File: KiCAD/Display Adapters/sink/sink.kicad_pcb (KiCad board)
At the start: 4 copper layers, 36.4 x 30.5 mm, 7 parts, among them J1 XT30PW_2_2_-M.G.B, J2 G46M2013201AWEU, J3 20455-040E-76

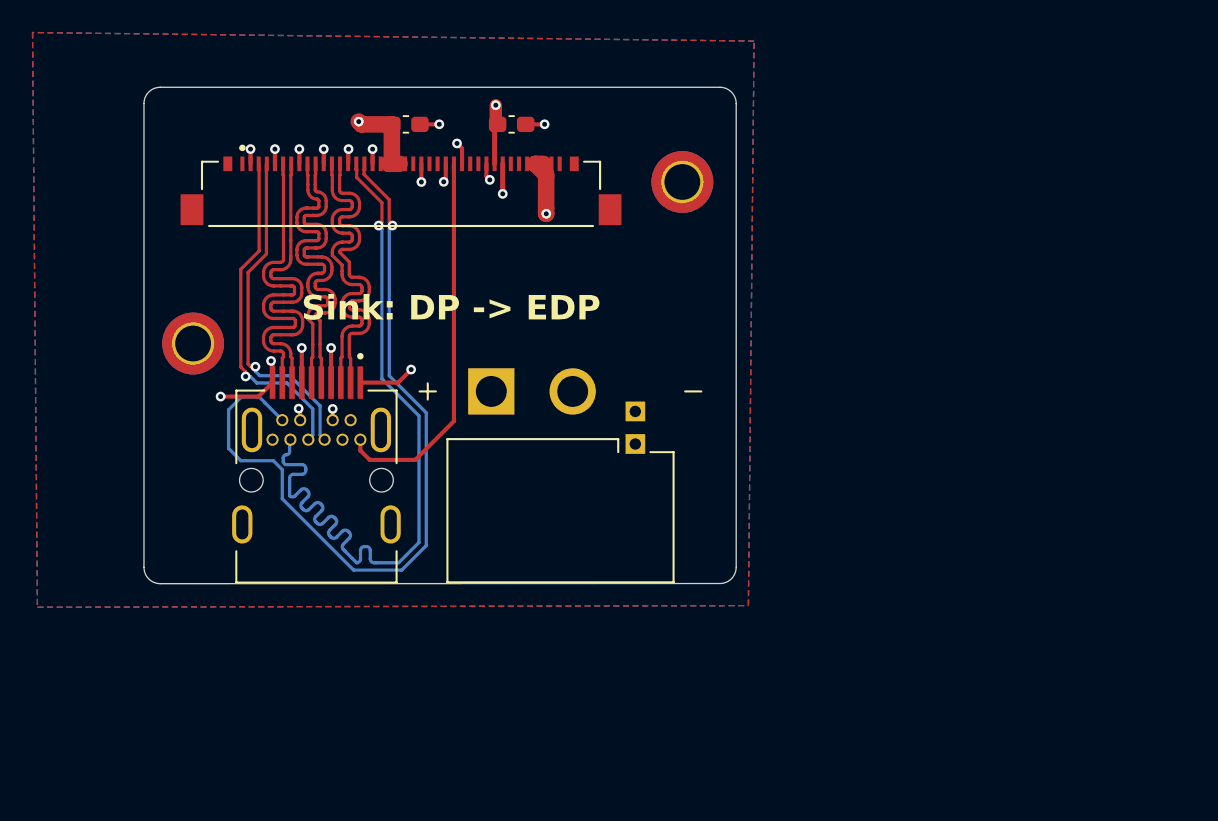
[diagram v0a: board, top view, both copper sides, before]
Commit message: use full sized dp instead
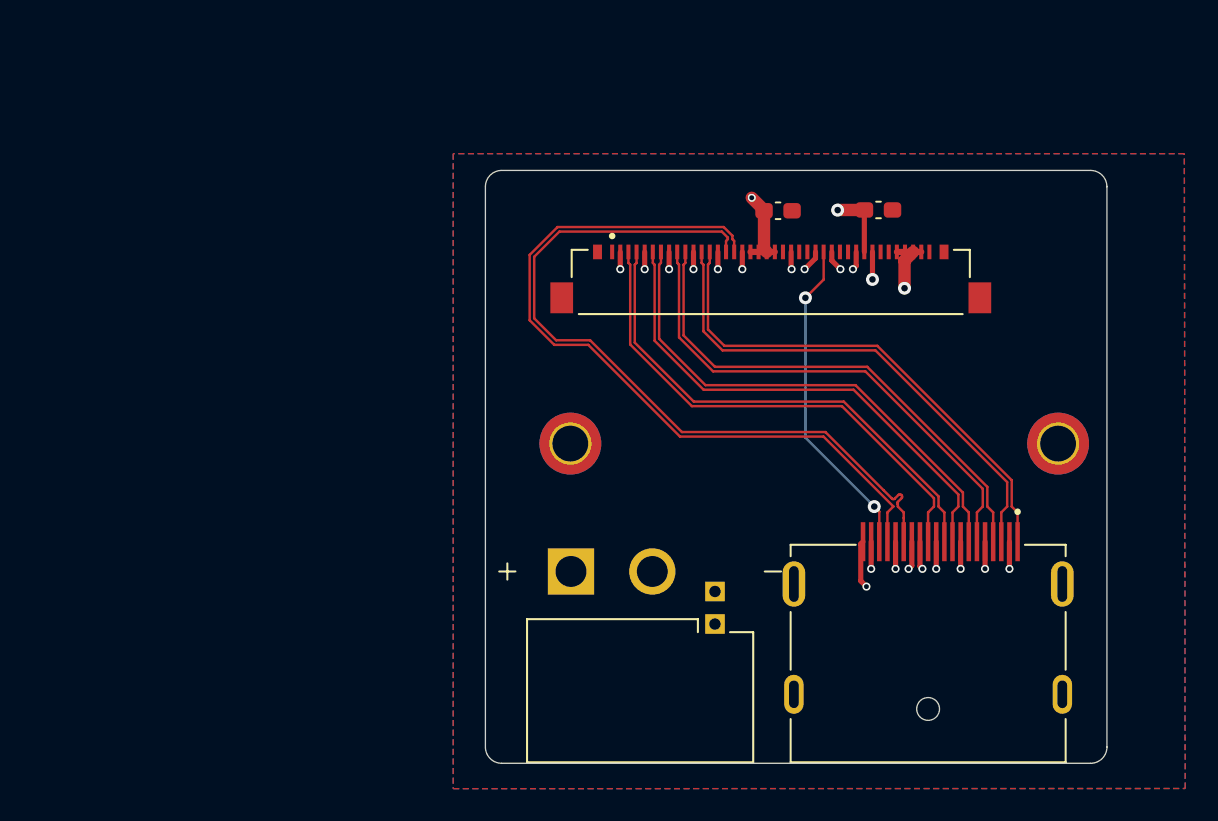
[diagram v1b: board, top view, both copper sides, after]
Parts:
- J1: value XT30PW_2_2_-M.G.B -> 47272-0001; footprint SnapEDA:AMASS_XT30PW_2_2_-M.G.B -> SnapEDA:MOLEX_47272-0001
- J2: value G46M2013201AWEU -> XT30PW_2_2_-M.G.B; footprint SnapEDA:AMPHENOL_G46M2013201AWEU -> SnapEDA:AMASS_XT30PW_2_2_-M.G.B
- moved H2 28.1 mm to (187.2, 106.8)
- moved J1 27.4 mm to (179.2, 126.4)
- moved H1 24.0 mm to (157.2, 106.8)
- moved J2 23.7 mm to (161.5, 122.0)
- moved C1 23.5 mm to (170.0, 92.5)
- moved J3 23.4 mm to (169.6, 96.9)
- moved C2 23.2 mm to (176.2, 92.4)
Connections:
- J1 pad S1: BLK_PWM_LCD -> GND
- J1 pad S2: BLK_OFF_N -> GND
- J2 pad S1: GND -> BLK_OFF_N
- J2 pad S2: GND -> BLK_PWM_LCD
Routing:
- net 0_EDP_TX_P: track 20.5 -> 31.2 mm
- net 0_EDP_TX_N: track 20.5 -> 31.2 mm
- net 3_EDP_TX_N: track 20.6 -> 31.1 mm, vias 1 -> 0
- net 3_EDP_TX_P: track 20.6 -> 31.1 mm, vias 1 -> 0
- net 1_EDP_TX_N: track 20.8 -> 31.2 mm
- net 1_EDP_TX_P: track 20.8 -> 31.2 mm
- net 2_EDP_TX_P: track 21.5 -> 31.1 mm
- net 2_EDP_TX_N: track 21.5 -> 31.1 mm
- net +5V: track 41.9 -> 48.6 mm
- net BLK_OFF_N: track 29.5 -> 35.4 mm
- net +3.3V: track 12.0 -> 8.17 mm, vias 1 -> 2
- net GND: track 28.6 -> 24.7 mm, vias 19 -> 18
- net EDP_HPD: track 23.5 -> 20.2 mm, vias 0 -> 2
- net BLK_PWM_LCD: track 24.0 -> 25.2 mm
- net AUX_N: track 48.8 -> 47.9 mm, vias 1 -> 0
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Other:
- board size 36.4 x 30.5 mm -> 38.2 x 36.4 mm
- board text removed: "Sink: DP -> EDP"
